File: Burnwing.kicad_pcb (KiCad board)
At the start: 4 copper layers, 50.8 x 22.9 mm, 49 parts, among them J1 USB Type C, J2 Conn_01x06_MountingPin, J4 Conn_01x04_Pin, Q2 AONR21307, SW1 SW_DIP_x02, U1 HUSB238, U2 BTS7030-2EPA

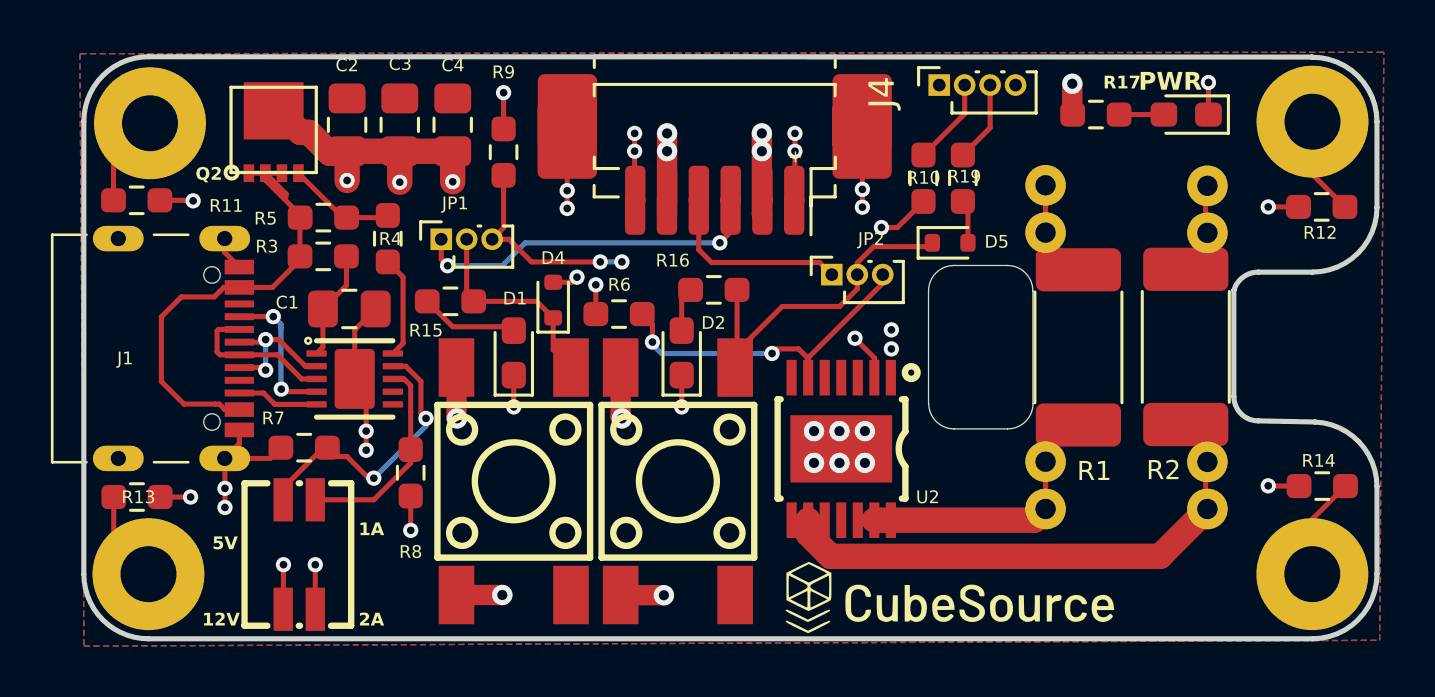
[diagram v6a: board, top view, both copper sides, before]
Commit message: Changed jumper headers
Changed jumper pins to 1.27 size
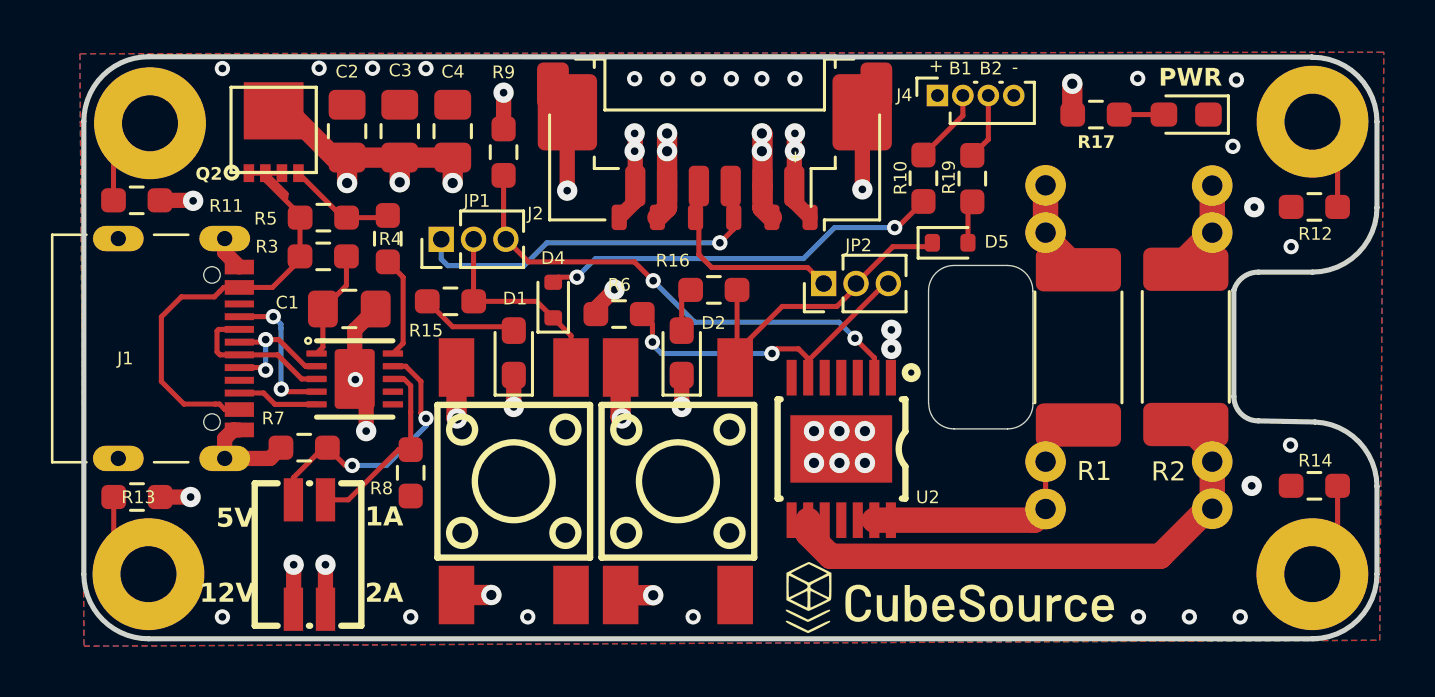
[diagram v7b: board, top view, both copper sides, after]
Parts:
- Burn1, Burn2: footprint EasyEDA:KEY-SMD_4P-L6.0-W6.0-P4.50-LS9.5-BR -> Library:KEY-SMD_4P-L6.0-W6.0-P4.50-LS9.5-BR
- D4, D5: footprint Diode_SMD:D_SOD-523 -> Library:D_SOD-523
- J2: value Conn_01x06_MountingPin -> C563981
- J2: footprint Library:Molex_PicoBlade_53261-0671_1x06-1MP_P1.25mm_Horizontal -> Library:Molex_Pico-Lock_504050-0691_1x06-1MP_P1.50mm_Horizontal
- J4: footprint Connector_PinSocket_1.00mm:PinSocket_1x04_P1.00mm_Vertical -> Library:PinSocket_1x04_P1.00mm_Vertical
- JP1, JP2: footprint Connector_PinSocket_1.00mm:PinSocket_1x03_P1.00mm_Vertical -> Library:PinHeader_1x03_P1.27mm_Vertical
- U2: footprint EasyEDA:PG-TSDSO-14_L4.9-W3.9-P0.65-LS6.0-BL-EP -> Library:PG-TSDSO-14_L4.9-W3.9-P0.65-LS6.0-BL-EP
- moved JP2 0.47 mm to (106.6, 89.0)
- moved J4 0.42 mm to (111.1, 81.6)
- moved SW1 0.40 mm to (86.4, 99.6)
- moved R19 0.37 mm to (112.5, 84.8)
- moved R14 0.31 mm to (125.9, 96.9)
- moved R12 0.29 mm to (125.9, 85.9)
- moved J2 0.28 mm to (102.3, 83.6)
- moved C2 0.25 mm to (87.9, 83.0)
- moved C3 0.25 mm to (90.0, 83.0)
- moved C4 0.25 mm to (92.0, 83.0)
- moved R2 0.19 mm to (121.9, 91.5)
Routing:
- net GND: track 48.3 -> 41.7 mm, vias 26 -> 42
- net Net-(H2-Pad1): track 2.78 -> 4.74 mm
- net Net-(R2-Pad2): track 21.0 -> 22.6 mm
- net Net-(D4-A): track 17.1 -> 15.9 mm
- net BURN_CTRL_1: track 13.5 -> 14.7 mm, vias 2 -> 1
- net VDC: track 27.2 -> 26.3 mm
- net BURN_CTRL_2: track 7.28 -> 8.05 mm
- net Net-(H4-Pad1): track 2.81 -> 3.56 mm
- net Net-(U1-VSET): track 8.20 -> 7.49 mm
- net /GATE1: track 20.2 -> 19.5 mm, vias 3 -> 2
- net Net-(U1-ISET): track 11.3 -> 10.7 mm
- net MICRO_BURN_2: track 3.19 -> 2.61 mm
- net Net-(Burn2-C): track 13.8 -> 13.3 mm
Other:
- board text added: "-"
- board text added: "B1"
- board text added: "B2"
